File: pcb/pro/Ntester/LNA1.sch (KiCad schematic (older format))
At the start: 21 parts, among them Q2 BC847BDW1T1G, U5 LT1818

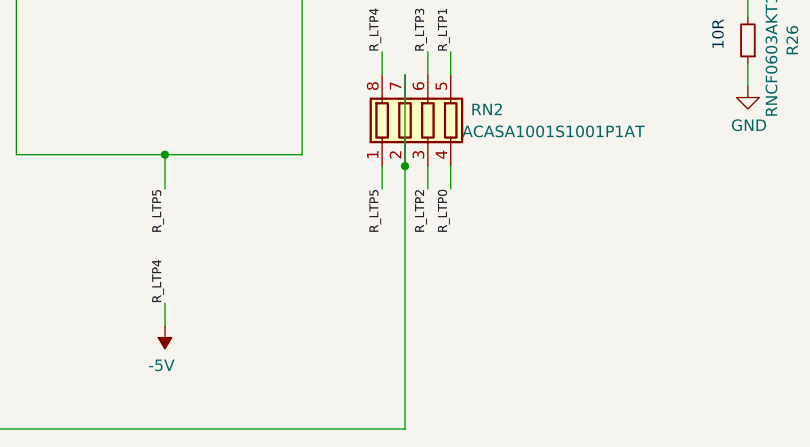
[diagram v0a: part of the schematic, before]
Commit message: BOM was updated
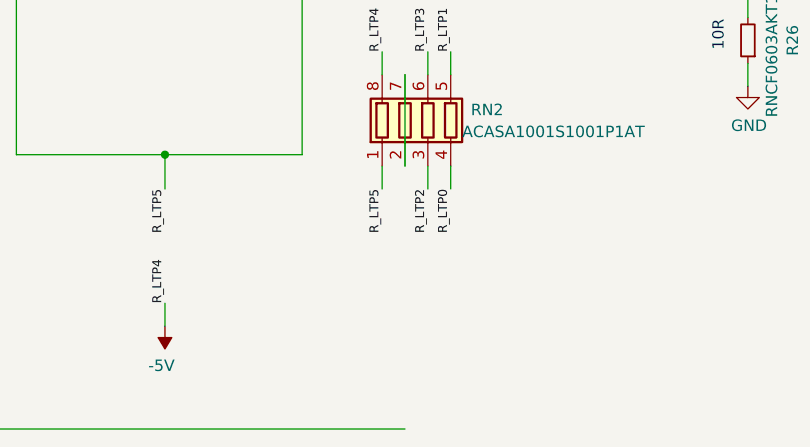
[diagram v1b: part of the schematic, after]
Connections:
- net IN_AMP: no longer RN2.2 (R2.1), RN2.7 (R2.2)
- new net: RN2.2 (R2.1), RN2.7 (R2.2)
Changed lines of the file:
@@
 	4600 4650 4600 5050
-Wire Wire Line
-	4600 5050 4600 6200
 Wire Wire Line
 	4600 6200 2500 6200
 Wire Wire Line
 	2500 6200 2500 4100
-Connection ~ 4600 5050
 Connection ~ 2500 4100
 Wire Wire Line
